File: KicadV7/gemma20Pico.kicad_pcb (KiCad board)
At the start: 2 copper layers, 60 x 45 mm, 13 parts, among them J1-Prox1 I2C_CH0, J2-Prox0 I2C_CH1, J3-Motor1 DC-Motor, J4-BAT1 3.7V Battery, J5-Servo1 Servo, J6-Pot1 Pot, J7-Pot2 Pot, U1-RPI-Pico1 Pico

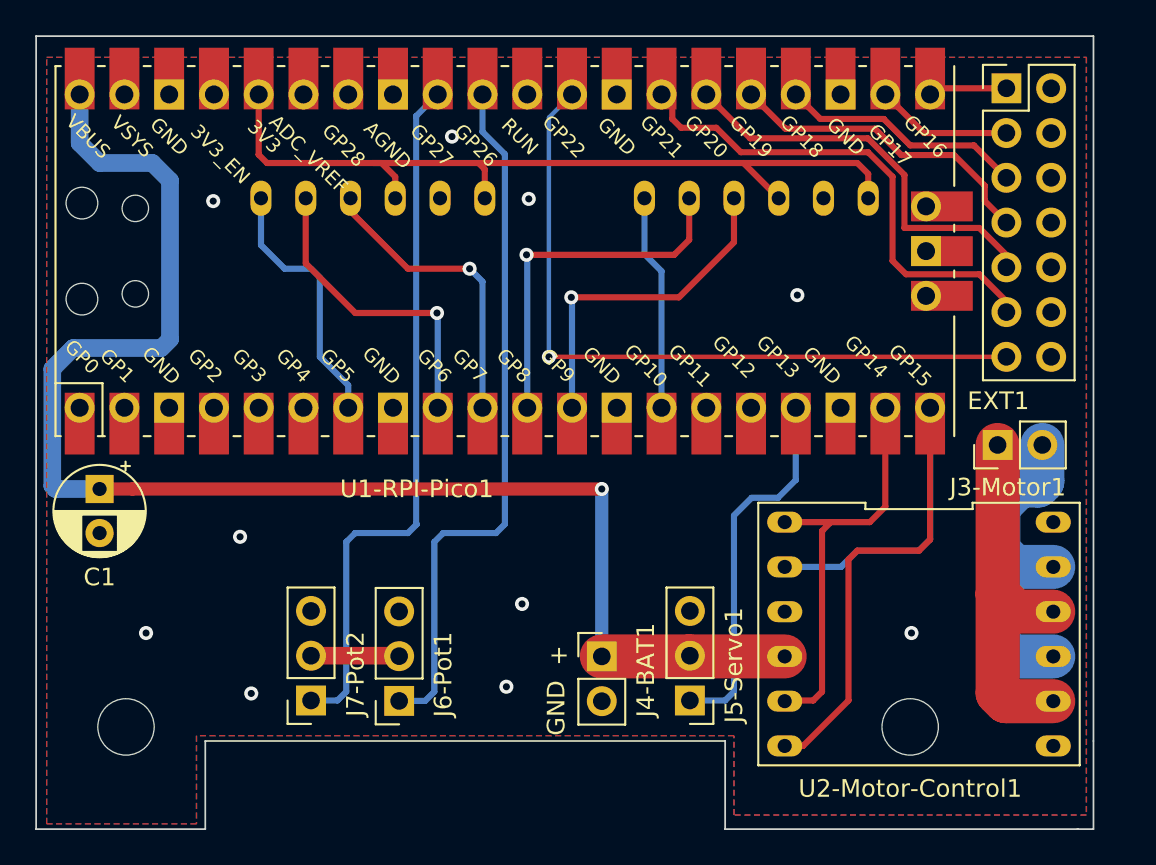
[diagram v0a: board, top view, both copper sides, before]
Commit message: Added ECS Pins & cleanup
Added ECS connector allows the DRV8833 to be replaced  with brushless motor controller for RC (also provides +5v)
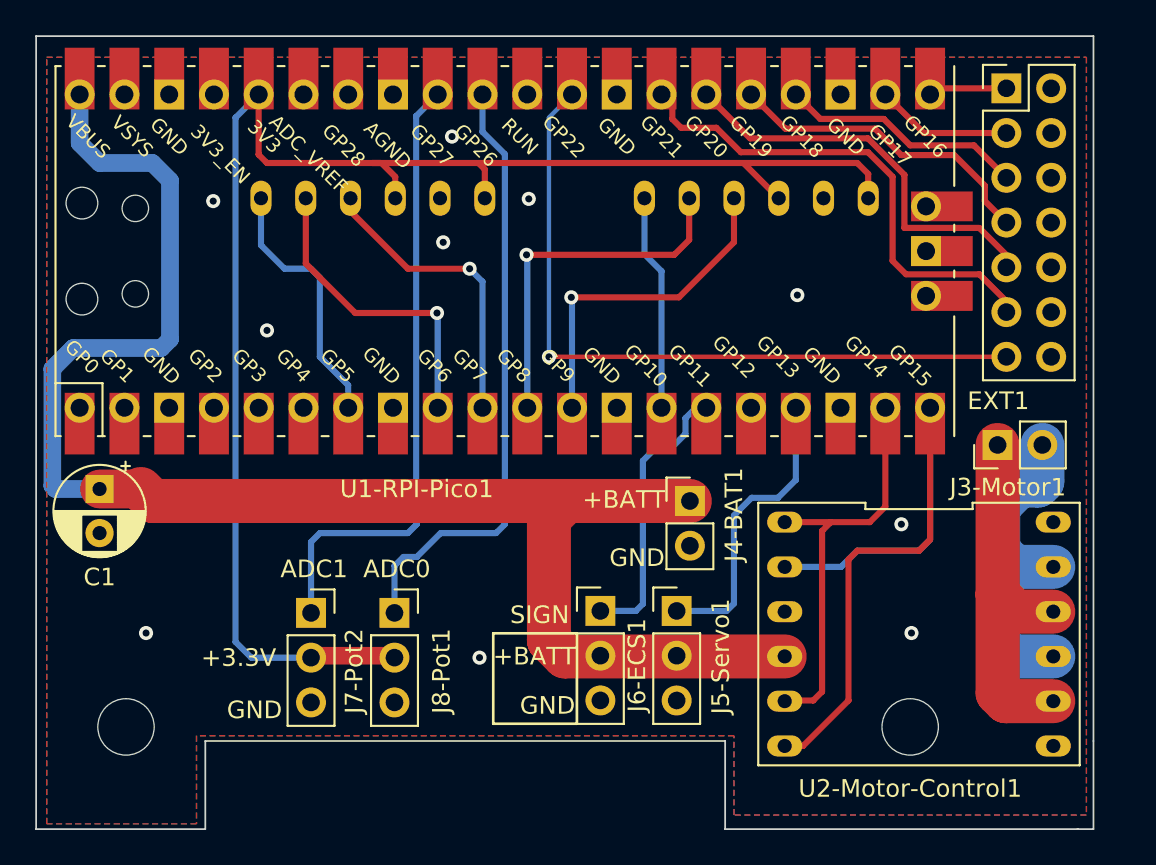
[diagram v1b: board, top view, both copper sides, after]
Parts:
- added J6-ECS1: ECS/Servo, Connector_PinHeader_2.54mm:PinHeader_1x03_P2.54mm_Vertical, F.Cu at (121.9, 112.9)
- moved J4-BAT1 10.1 mm to (127.0, 106.7)
- moved J5-Servo1 5.14 mm to (126.2, 112.9), turned to 0 degrees
- moved J8-Pot1 5.00 mm to (110.2, 113.0), turned to 0 degrees
- moved J7-Pot2 4.97 mm to (105.5, 113.0), turned to 0 degrees
- renumbered J6-Pot1 to J8-Pot1
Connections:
- U1-RPI-Pico1 pad 15: unconnected-(U1-RPI-Pico1-GPIO11-Pad15) -> /ECS_SIGN
- U1-RPI-Pico1 pad 33: unconnected-(U1-RPI-Pico1-AGND-Pad33) -> GND
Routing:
- net +3.3V: track 52.7 -> 88.9 mm
- net /ECS_SIGN: track 0.00 -> 16.1 mm
- net +BATT: track 82.9 -> 90.4 mm, vias 1 -> 0
- net /ADC0: track 40.0 -> 34.8 mm
- net /ADC1: track 41.7 -> 37.0 mm
- net /Servo_SIGN: track 21.1 -> 16.9 mm
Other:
- board text added: "+3.3V"
- board text added: "+BATT"
- board text added: "16"
- board text added: "19"
- board text added: "20"
- board text added: "ADC0"
- board text added: "ADC1"
- board text added: "GP17"
- board text added: "GP18"
- board text added: "GP21"
- board text added: "GP22"
- board text added: "SIGN"
- board text removed: "+"

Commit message: Reduced Size to better fir the new gamma2.0
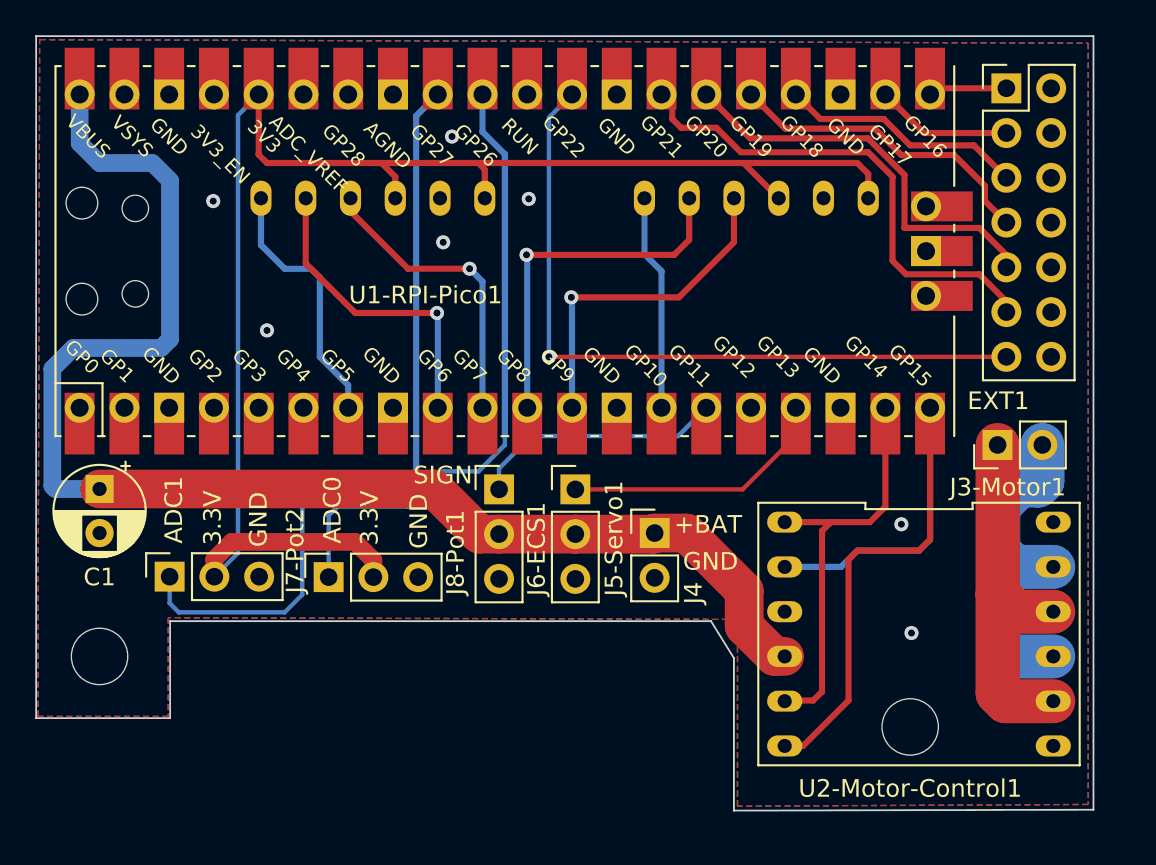
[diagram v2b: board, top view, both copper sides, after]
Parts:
- moved J5-Servo1 8.98 mm to (120.5, 106.0)
- moved J6-ECS1 8.98 mm to (116.2, 106.0)
- moved J7-Pot2 8.28 mm to (97.5, 111.0), turned to 90 degrees
- moved REF** 4.27 mm to (93.5, 115.5)
- moved J8-Pot1 4.25 mm to (106.5, 111.0), turned to 90 degrees
- moved J4 2.70 mm to (125.0, 108.5)
- renumbered J4-BAT1 to J4
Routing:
- net +BATT: track 90.4 -> 78.6 mm
- net /ADC1: track 37.0 -> 45.5 mm
- net /ECS_SIGN: track 16.1 -> 14.4 mm
- net /Servo_SIGN: track 16.9 -> 15.4 mm
- net +3.3V: track 88.9 -> 87.9 mm
- net /ADC0: track 34.8 -> 35.6 mm
- net GND: vias 10 -> 7
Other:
- board size 60 x 45 mm -> 60 x 44 mm
- board text added: "+BAT"
- board text added: "3.3V"
- board text added: "PicoRC 1.2 USN 2023"
- board text removed: "+3.3V"
- board text removed: "+BATT"
- board text removed: "PicoRC 1.1 USN 2023"

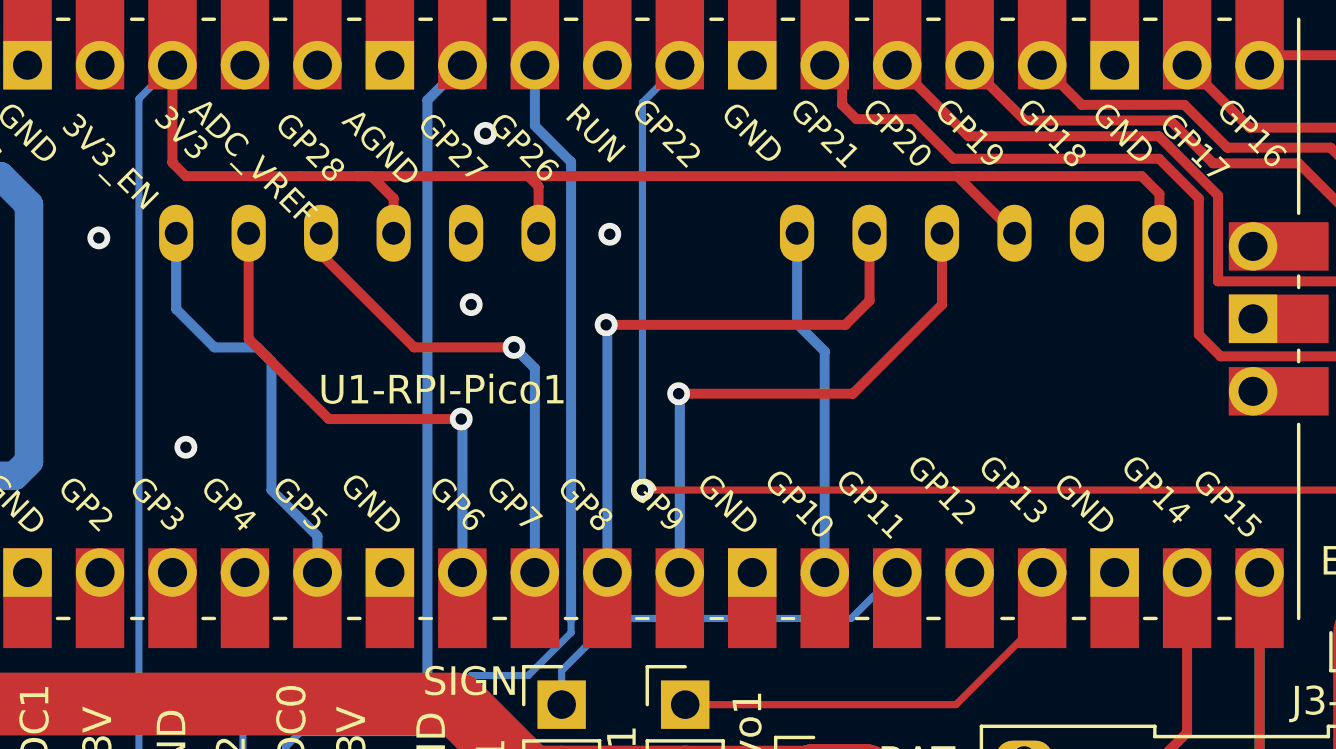
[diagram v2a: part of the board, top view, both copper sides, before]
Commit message: Fix Footprit Pox sensors was not updated
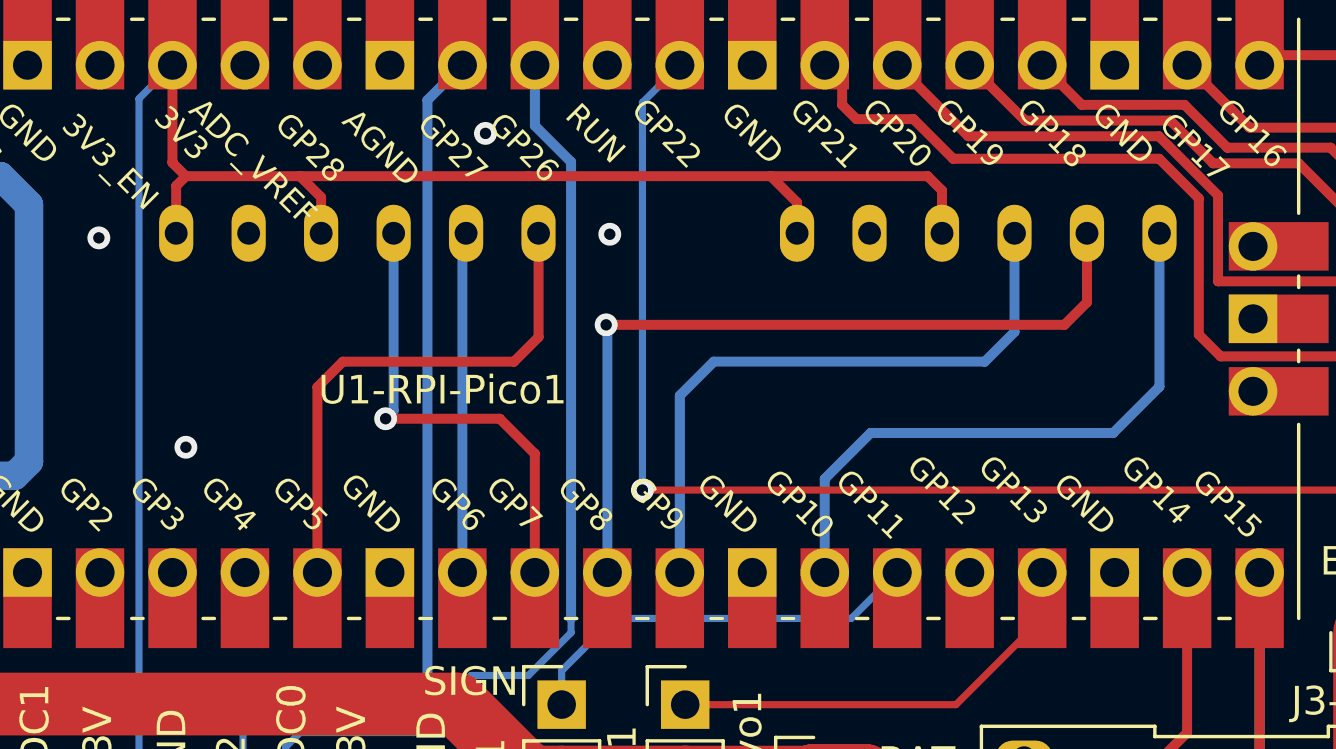
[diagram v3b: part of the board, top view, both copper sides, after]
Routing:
- net /INT0: track 12.3 -> 21.7 mm
- net +3.3V: track 87.9 -> 79.4 mm
- net /SDA0: track 20.6 -> 28.3 mm
- net /SDA1: track 17.7 -> 11.9 mm, vias 1 -> 0
- net /INT1: track 14.8 -> 18.6 mm
- net /SCL0: track 19.3 -> 22.3 mm, vias 1 -> 0
- net /SCL1: track 17.0 -> 16.5 mm
- net GND: track 0.18 -> 0.00 mm, vias 7 -> 6
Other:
- board text added: "PicoRC 1.3 USN 2023"
- board text removed: "PicoRC 1.2 USN 2023"
